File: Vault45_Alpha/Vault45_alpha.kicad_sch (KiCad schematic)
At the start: 139 parts, among them J1 AVR-ISP-6, SW1 SW_PUSH, SW2 SW_PUSH, SW3 RotaryEncoder_Switch, U1 SRV05-4, U2 ATmega32U4-M, X1 Crystal_GND24_Small

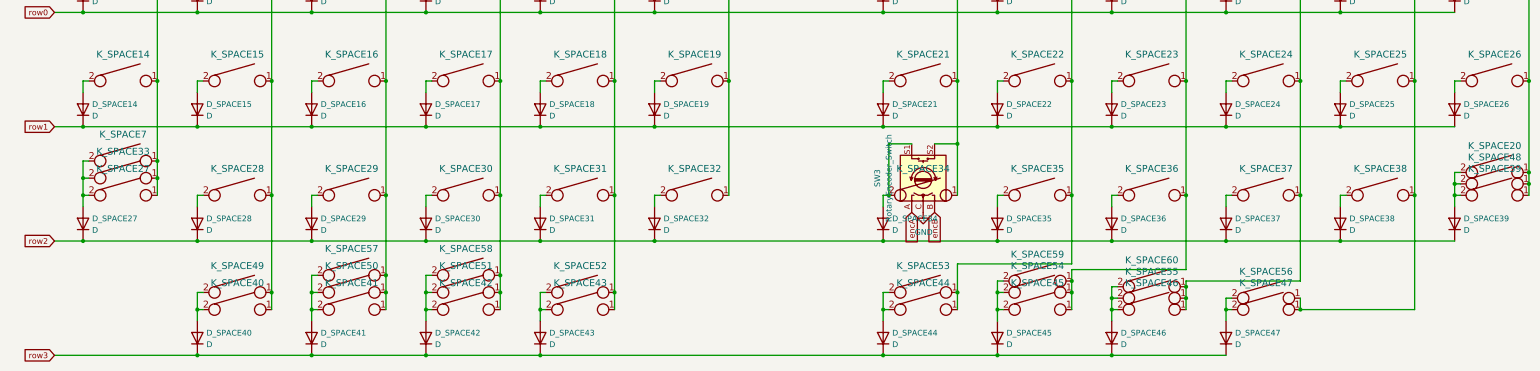
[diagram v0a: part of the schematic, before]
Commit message: updated pcb layout to address interference with plate mounting hardware and added custom plate files
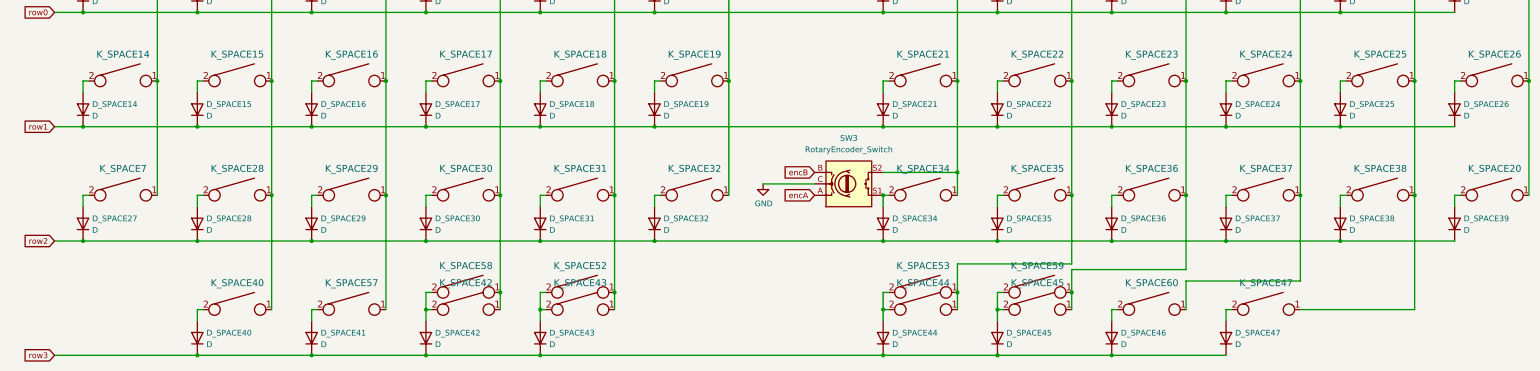
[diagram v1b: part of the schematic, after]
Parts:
- removed K_SPACE27, K_SPACE39, K_SPACE41, K_SPACE46, K_SPACE50, K_SPACE51, K_SPACE54, K_SPACE55: KEYSW, MX_Only:MXOnly-1U-NoLED, symbol keyboard_parts:KEYSW
- removed K_SPACE33, K_SPACE48: KEYSW, MX_Only:MXOnly-1.25U-NoLED, symbol keyboard_parts:KEYSW
- removed K_SPACE49, K_SPACE56: KEYSW, MX_Only:MXOnly-1.75U-NoLED, symbol keyboard_parts:KEYSW
- K_SPACE40, K_SPACE47: footprint MX_Only:MXOnly-1.25U-NoLED -> MX_Only:MXOnly-1U-NoLED
- K_SPACE52, K_SPACE53: footprint MX_Only:MXOnly-1.5U-NoLED -> MX_Only:MXOnly-2U-ReversedStabilizers-NoLED
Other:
- moved on the sheet: K_SPACE20, K_SPACE57, K_SPACE58, K_SPACE59, K_SPACE60, K_SPACE7, SW3

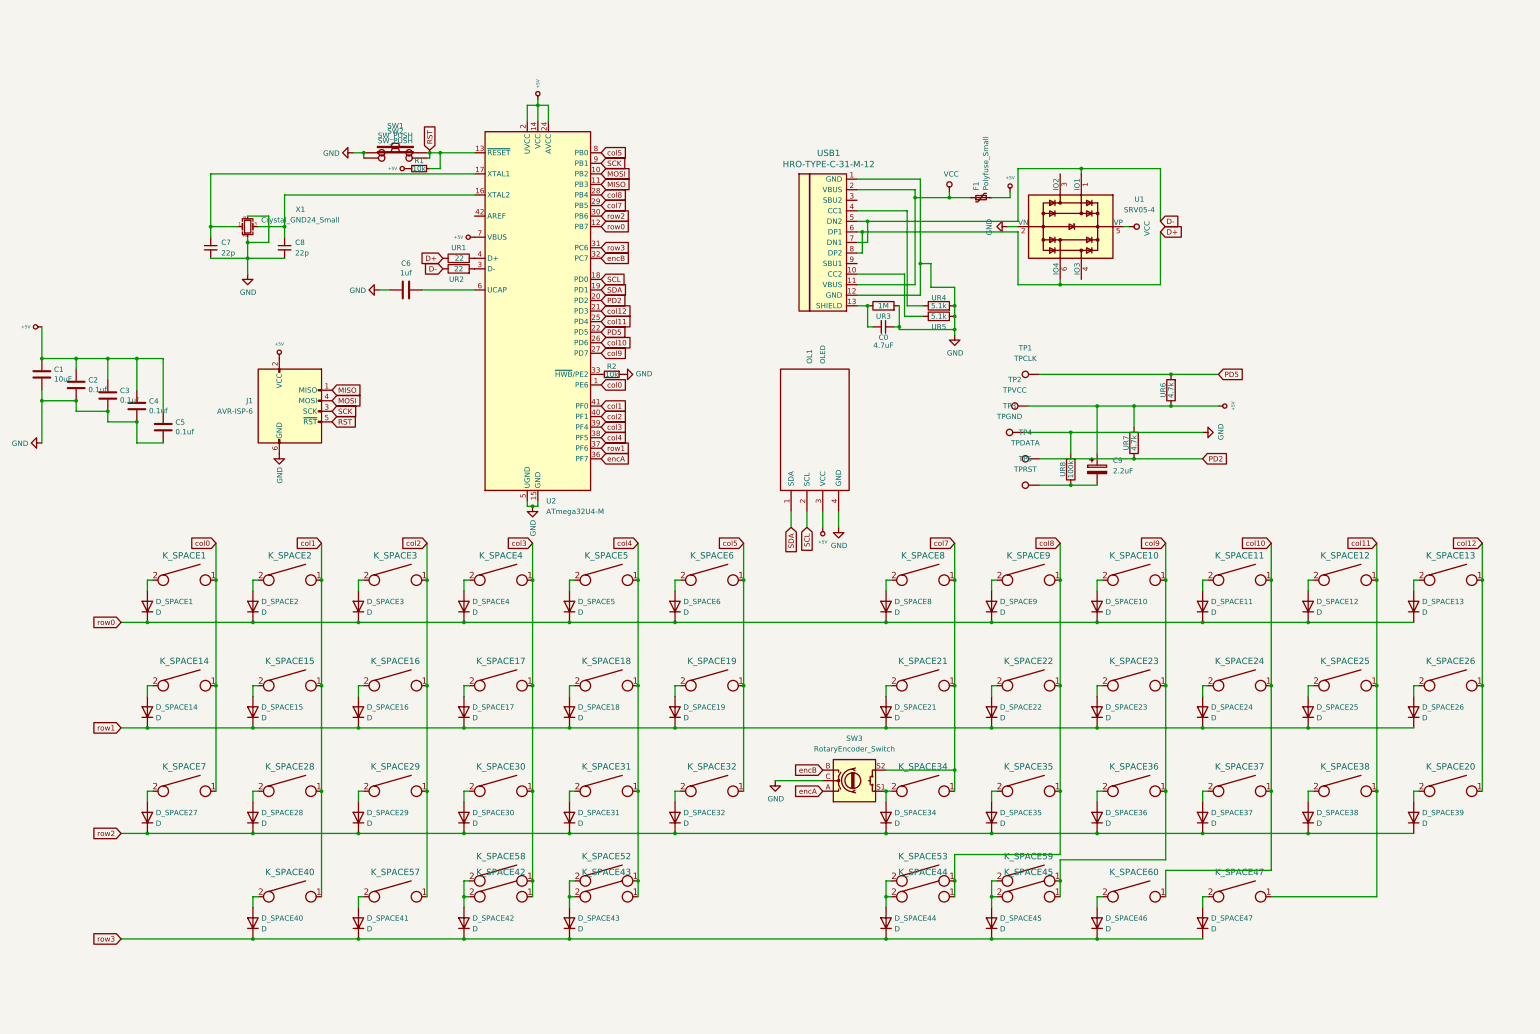
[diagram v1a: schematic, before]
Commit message: Added bottom row options to Vault 45 Alpha PCB and updated fabrication files.
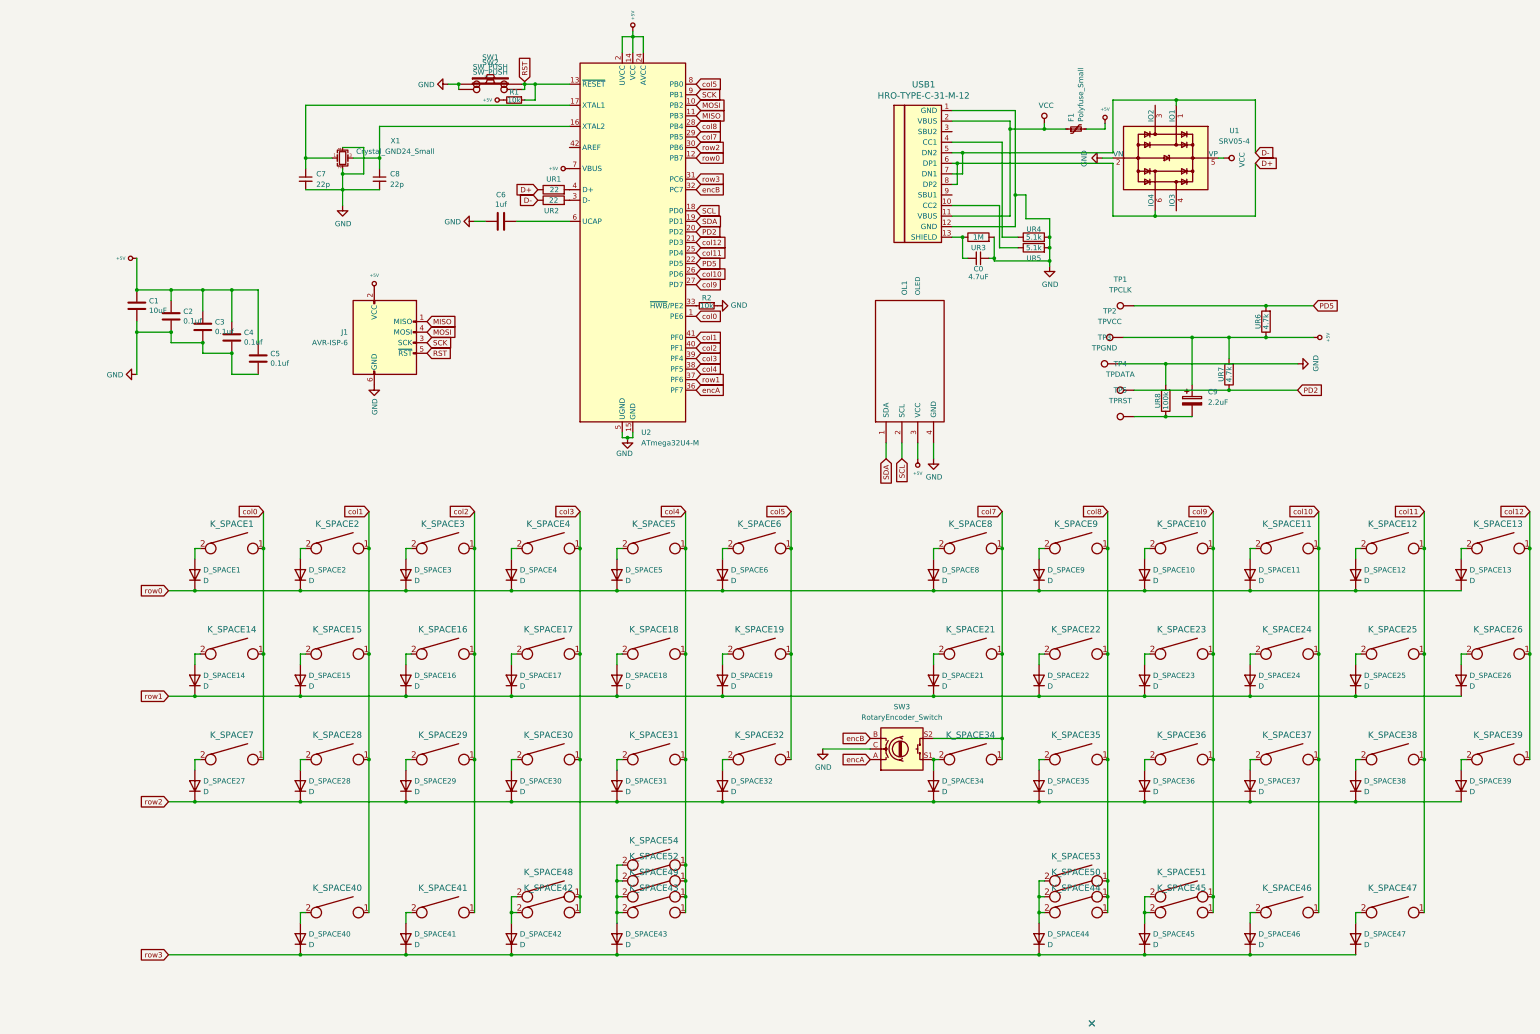
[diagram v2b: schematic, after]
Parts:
- added K_SPACE52, K_SPACE53: KEYSW, MX_Only:MXOnly-3U-ReversedStabilizers-NoLED, symbol keyboard_parts:KEYSW
- added K_SPACE54: KEYSW, MX_Only:MXOnly-4U-ReversedStabilizers-NoLED, symbol keyboard_parts:KEYSW
- renumbered K_SPACE20 to K_SPACE39, K_SPACE57 to K_SPACE41, K_SPACE60 to K_SPACE46, K_SPACE58 to K_SPACE48, K_SPACE52 to K_SPACE49, K_SPACE53 to K_SPACE50, K_SPACE59 to K_SPACE51
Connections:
- net col4: now also K_SPACE52.1, K_SPACE54.1
- net col8: now also K_SPACE53.1
- net at D_SPACE43.2 (A), K_SPACE43.2, K_SPACE49.2: now also K_SPACE52.2, K_SPACE54.2
- net at D_SPACE44.2 (A), K_SPACE44.2, K_SPACE50.2: now also K_SPACE53.2
- no-connect marks 0 -> 1
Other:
- moved on the sheet: C0, C1, C2, C3, C4, C5, C6, C7, C8, C9, D_SPACE1, D_SPACE10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
